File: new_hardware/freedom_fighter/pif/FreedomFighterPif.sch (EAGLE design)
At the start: 15 parts, among them U1 PIA6821, U4 HD68A09EP, U5 74LS74D, U9 DM74LS04N

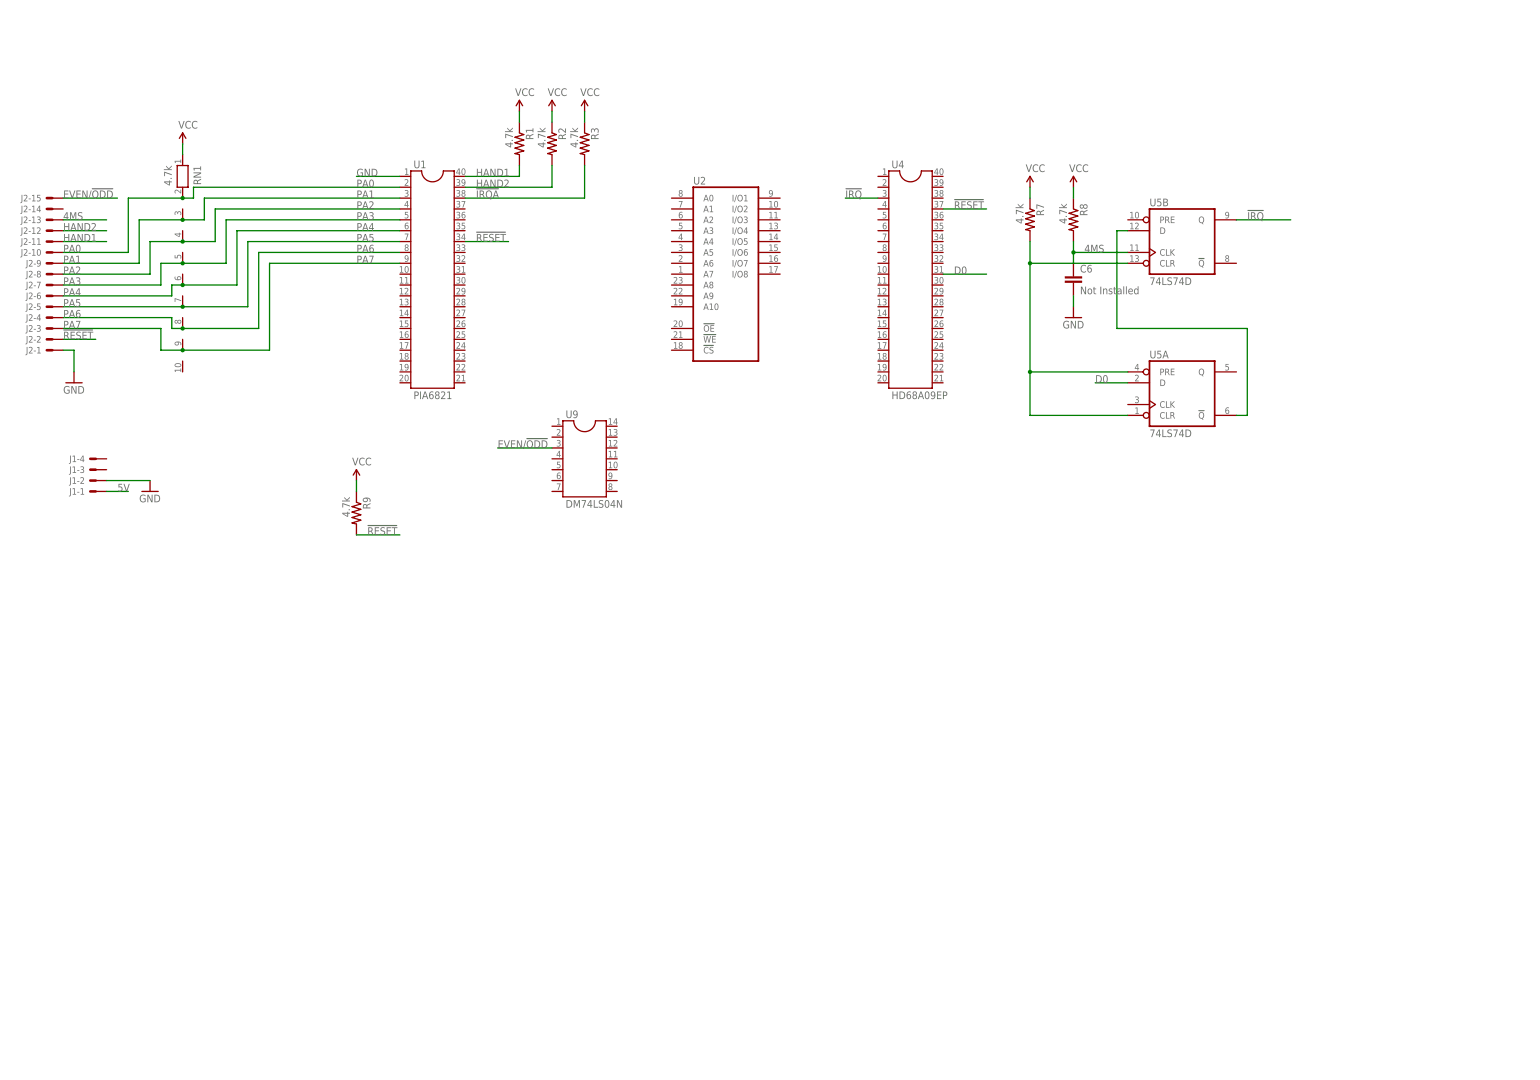
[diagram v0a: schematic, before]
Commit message: did more reverse engineering of freedom fighter pif board
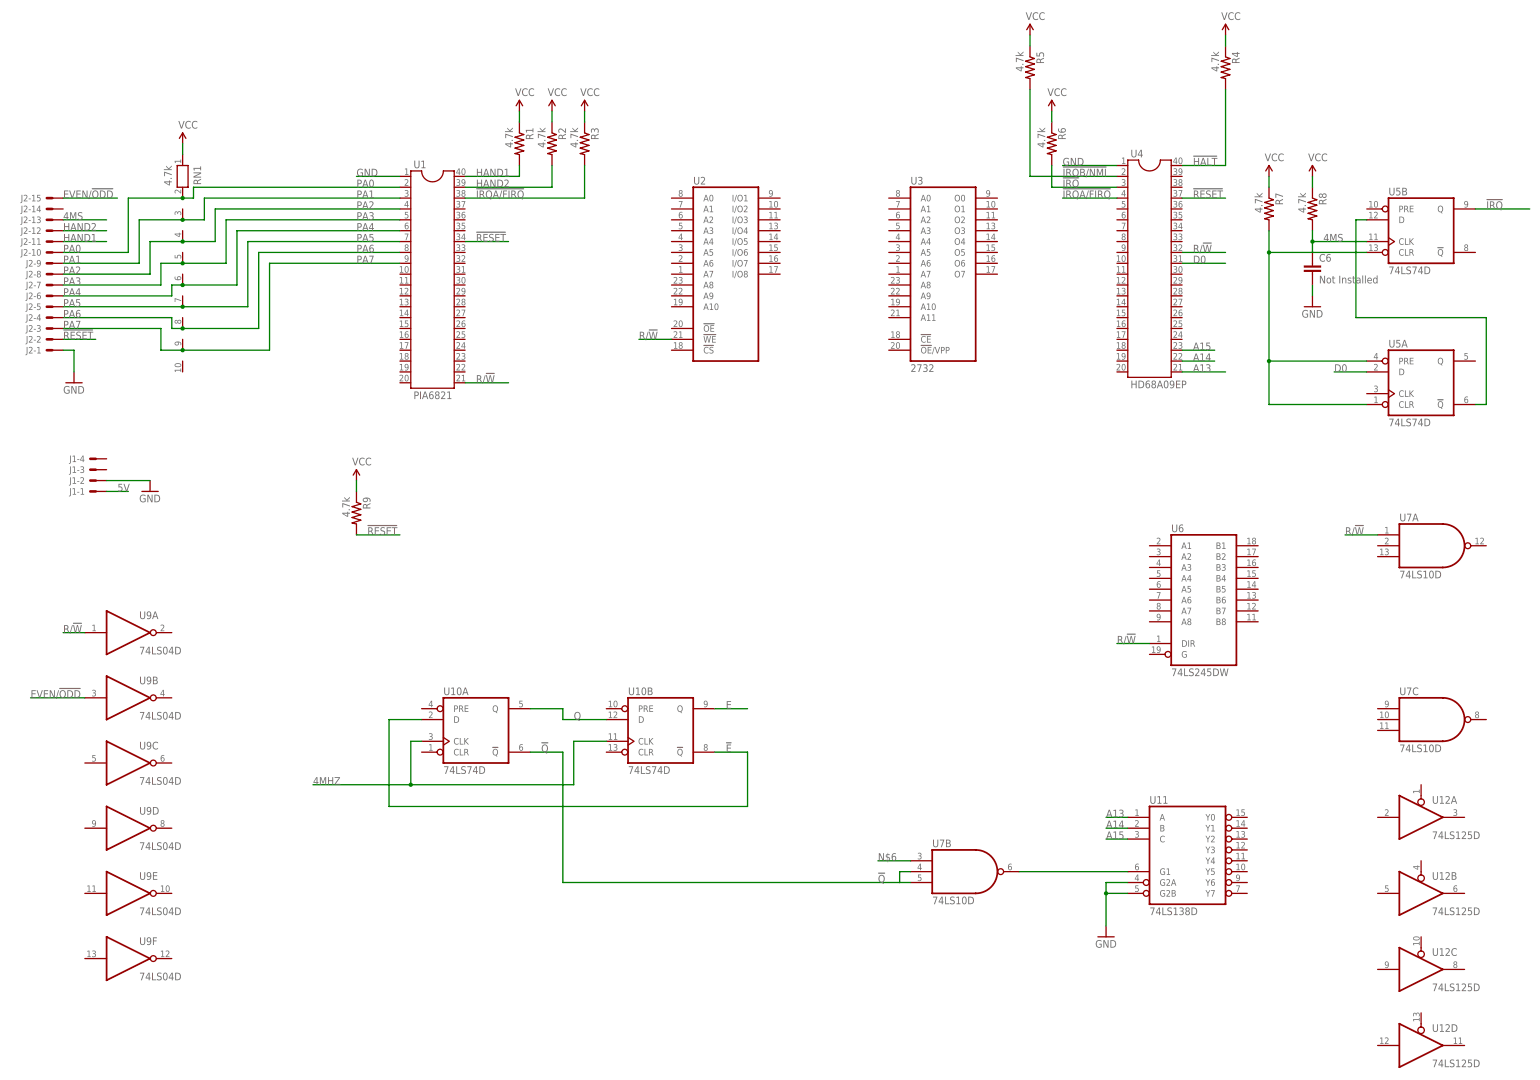
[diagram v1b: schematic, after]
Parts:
- added R4, R5, R6: 4.7k, SparkFun:RESISTOR1206
- added U10: 74LS74D, 74xx-us:74LS74D
- added U11: 74LS138D, 74xx-us:74LS138D
- added U12: 74LS125D, 74xx-eu:74LS125D
- added U3: 2732, memory:2732
- added U6: 74LS245DW, 74xx-us:74LS245DW
- added U7: 74LS10D, 74xx-us:74LS10D
- U9: value DM74LS04N -> 74LS04D; device ic-package:DIL14 -> 74xx-us:74LS04D
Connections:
- removed net !IRQA: R3.2, U1.38
- new net !E: U10A.D, U10B.!Q
- new net !HALT: R4.2, U4.40
- new net !IRQA/FIRQ: R3.2, U1.38, U4.4
- new net !IRQB/NMI: R5.2, U4.2
- new net !Q: U10A.!Q, U7B.I1, U7B.I2
- new net 4MHZ: U10A.CLK, U10B.CLK
- new net A13: U11A.A, U4.21
- new net A14: U11A.B, U4.22
- new net A15: U11A.C, U4.23
- new net E: U10B.Q
- new net N$4: U11A.G1, U7B.O
- new net N$6: U7B.I0
- new net Q: U10A.Q, U10B.D
- new net R/!W: U1.21, U2G$1.!WE, U4.32, U6A.DIR, U7A.I0, U9A.I
- net !IRQ: now also R6.2
- net EVEN/!ODD: now also U9B.I; no longer U9.3
- net GND: now also U11A.G2A, U11A.G2B, U4.1
- net VCC: now also R4.1, R5.1, R6.1
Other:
- moved on the sheet: C6, R7, R8, U4, U5A, U5B

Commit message: more reverse engineering
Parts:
- removed U3: 2732, memory:2732
- added C100: Unknown value, SparkFun:CAP1206
- added DB1: DB25, mpo:A32077-ND
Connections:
- removed net N$6: U7B.I0
- new net !ENABLE_DAVDAK: U11A.Y1, U12A.OE, U12D.OE
- new net !ENABLE_PIA: U1.23, U11A.Y4
- new net !ENABLE_RAM: U11A.Y0, U2G$1.!CS
- new net !ENABLE_ROM: U11A.Y7, U12B.OE
- new net !ENABLE_ROM_CE: U12B.O
- new net !ENABLE_U12C: U11A.Y6, U12C.OE
- new net !ENABLE_VP931_DATA: U11A.Y3, U6A.G, U9D.I
- new net !VP931_RDEN: DB1.10, U7A.O
- new net !VP931_WREN: DB1.22, U7C.O
- new net D1: U4.30, U6A.B2
- new net D2: U4.29, U6A.B3
- new net D3: U4.28, U6A.B4
- new net D4: U4.27, U6A.B5
- new net D5: U4.26, U6A.B6
- new net D6: U12D.O, U4.25, U6A.B7
- new net D7: U12A.O, U4.24, U6A.B8
- new net ENABLE_VP931_DATA: U7A.I2, U7C.I1, U9D.O
- new net VP931_D0: DB1.14, U6A.A1
- new net VP931_D1: DB1.15, U6A.A2
- new net VP931_D2: DB1.16, U6A.A3
- new net VP931_D3: DB1.17, U6A.A4
- new net VP931_D4: DB1.18, U6A.A5
- new net VP931_D5: DB1.19, U6A.A6
- new net VP931_D6: DB1.20, U6A.A7
- new net VP931_D7: DB1.21, U6A.A8
- new net VP931_DAK: DB1.23, U12A.I
- new net VP931_DAV: DB1.11, U12D.I
- new net W/!R: U2G$1.!OE, U7C.I0, U9A.O
- net !E: now also U7B.I0
- net D0: now also U6A.B1
- net E: now also C100.2, U4.34, U7A.I1
- net GND: now also DB1.9, U12B.I, U12C.I, U5B.PRE
- net Q: now also U4.35, U7C.I2
- net VCC: now also C100.1
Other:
- note added: "N/C?"
- note added: "This circuit is installed but does nothing because pin 10 is grounded"
- note added: "U3 is a 27128D!"
- moved on the sheet: U11

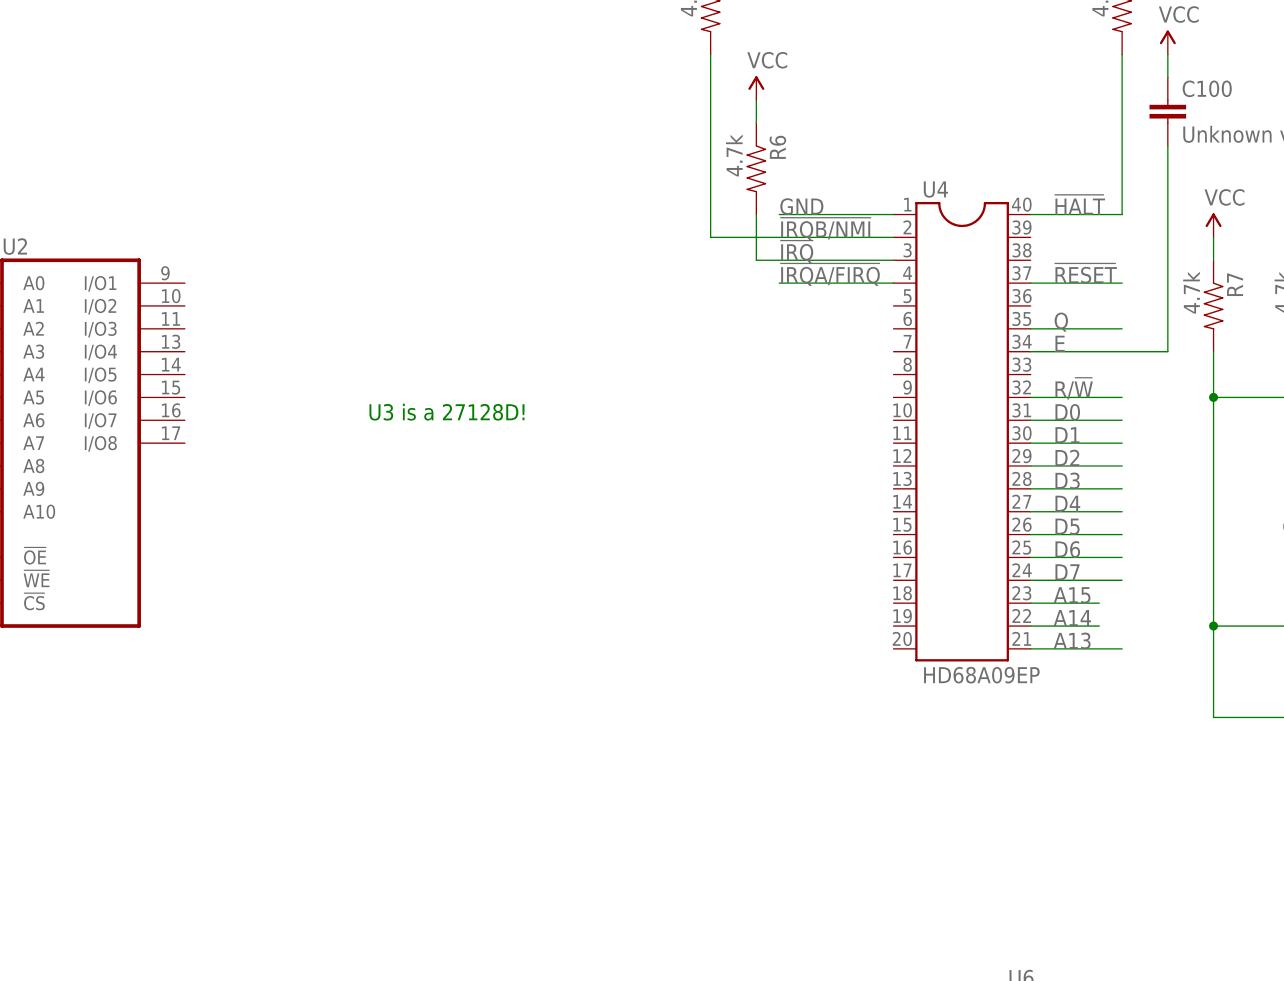
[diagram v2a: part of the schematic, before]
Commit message: added FFR PIF disassembly and updated PIF schematics
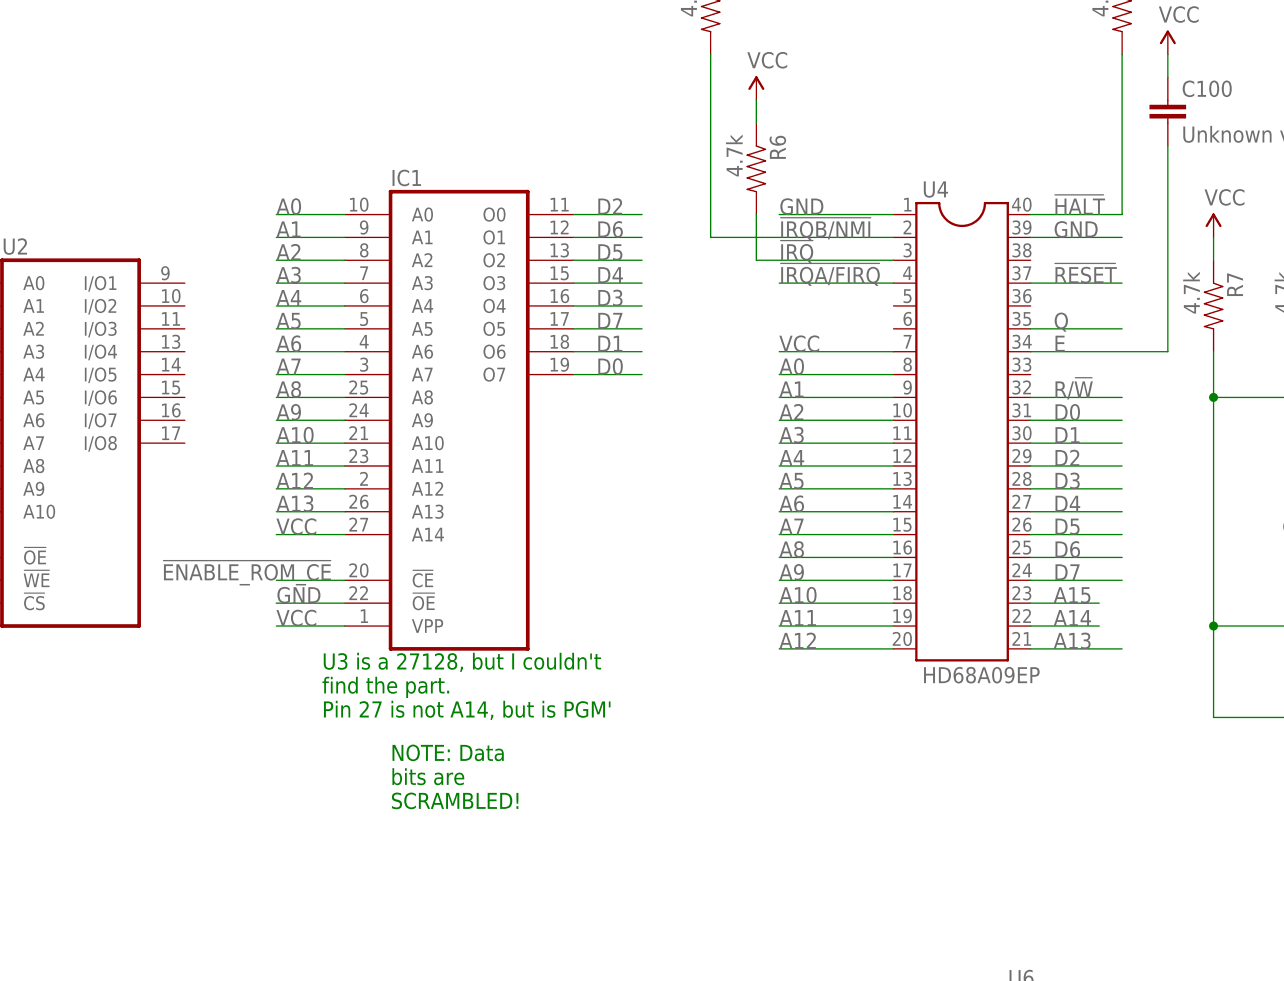
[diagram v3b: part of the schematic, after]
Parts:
- added IC1: (no value), memory:27256
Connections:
- new net A0: IC1A.A0, U4.8
- new net A1: IC1A.A1, U4.9
- new net A10: IC1A.A10, U4.18
- new net A11: IC1A.A11, U4.19
- new net A12: IC1A.A12, U4.20
- new net A2: IC1A.A2, U4.10
- new net A3: IC1A.A3, U4.11
- new net A4: IC1A.A4, U4.12
- new net A5: IC1A.A5, U4.13
- new net A6: IC1A.A6, U4.14
- new net A7: IC1A.A7, U4.15
- new net A8: IC1A.A8, U4.16
- new net A9: IC1A.A9, U4.17
- net !ENABLE_ROM_CE: now also IC1A.!CE
- net A13: now also IC1A.A13
- net D0: now also IC1A.O7
- net D1: now also IC1A.O6
- net D2: now also IC1A.O0
- net D3: now also IC1A.O4
- net D4: now also IC1A.O3
- net D5: now also IC1A.O2
- net D6: now also IC1A.O1
- net D7: now also IC1A.O5
- net GND: now also IC1A.!OE, U4.39
- net VCC: now also IC1A.A14, IC1A.VPP, U4.7
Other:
- note added: "NOTE: Data bits are SCRAMBLED!"
- note added: "U3 is a 27128, but I couldn't find the part. Pin 27 is not A14, but is PGM'"
- note removed: "U3 is a 27128D!"

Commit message: almost done with schematic, did some more disassembling
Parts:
- added C14, C9: 0.001uF, SparkFun:CAP1206
- added C15: 100uF/25V, SparkFun:CAP_POLPTH2
- added L1: 2.2uH, rcl:L-USTJ8-U2
- added R10, R11, R12: 4.7k, SparkFun:RESISTOR1206
- added X1: CRYSTAL OSC, crystal:TC46C
- DB1: value DB25 -> DB25 (FEMALE)
- U2: value (none) -> HM6116P-A
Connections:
- net !ENABLE_U12C renamed !ENABLE_ROM_C_TO_D
- removed net !ENABLE_ROM_CE: IC1A.!CE, U12B.O
- removed net 5V: J1-1.S
- new net !ENABLE_ROM_E_TO_F: U11A.Y7, U12B.OE
- new net CS0/CS1: R10.2, U1.22, U1.24
- new net N$5: R11.2, U10A.CLR, U10A.PRE, U10B.CLR, U10B.PRE
- new net N$8: C9.2, J1-1.S, L1.1
- net !ENABLE_ROM: now also IC1A.!CE, R12.2, U12B.O, U12C.O; no longer U11A.Y7, U12B.OE
- net !IRQB/NMI: now also U1.37
- net 4MHZ: now also X1.OUT
- net A0: now also U1.36, U2G$1.A0
- net A1: now also U1.35, U2G$1.A1
- net A10: now also U2G$1.A10
- net A2: now also U2G$1.A2
- net A3: now also U2G$1.A3
- net A4: now also U2G$1.A4
- net A5: now also U2G$1.A5
- net A6: now also U2G$1.A6
- net A7: now also U2G$1.A7
- net A8: now also U2G$1.A8
- net A9: now also U2G$1.A9
- net D0: now also U1.33, U2G$1.I/O1
- net D1: now also U1.32, U2G$1.I/O2
- net D2: now also U1.31, U2G$1.I/O3
- net D3: now also U1.30, U2G$1.I/O4
- net D4: now also U1.29, U2G$1.I/O5
- net D5: now also U1.28, U2G$1.I/O6
- net D6: now also U1.27, U2G$1.I/O7
- net D7: now also U1.26, U2G$1.I/O8
- net E: now also U1.25
- net GND: now also C14.1, C15.-, C9.1, X1.GND
- net VCC: now also C14.2, C15.+, L1.2, R10.1, R11.1, R12.1, U1.20, X1.VCC
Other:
- note added: "10-15 and 18-19 mirror Star Rider PIF exactly, going to an uninstalled 244. Pins 16-17 are N/C from what I can tell."
- note added: "Freedom Fighter PIF Prototype"
- note added: "I double checked: Pin 10 and Pin 13 are not connected"
- note added: "I partly guessed on the values for C9 and C14, and L1 by using Star Rider as reference."
- note added: "NOTE: DAV' is unconnected. This is opposite of Firefox, which uses DAV' but ignores DAV."
- note added: "NOTE: Data bits are SCRAMBLED (a simple type of obfuscation?)."
- note added: "NOTE: There is an uninstalled IC (U8) and uninstalled set of pin headers (J3) that look to be leftover from Star Rider's design. I did not bother with these since they were never used. They most likely mirror very closely the Star Rider PIF schematic."
- note added: "Oscillator is 4 MHz. I didn't try to find an exact match, just enough to document."
- note added: "Reverse engineered by Matt Ownby 2015"
- note added: "U3 is a 27128, but I couldn't find the part so I used a 27256. Pin 27 is not A14, but is PGM'"
- note removed: "NOTE: Data bits are SCRAMBLED!"
- note removed: "U3 is a 27128, but I couldn't find the part. Pin 27 is not A14, but is PGM'"
- moved on the sheet: C6, R7, R8, R9, U10A, U10B, U5A, U5B

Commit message: Essentially finished schematic, started laying out PCB
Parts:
- removed X1: CRYSTAL OSC, crystal:TC46C
- added C1, C10, C11, C12, C13, C2, C3, C4, C5, C7, C8: 0.1uF, SparkFun:CAP1206
- added JP1, JP4: (no value), pinhead:PINHD-1X20
- added JP2, JP5, JP6: (no value), pinhead:PINHD-1X8
- added JP3: (no value), pinhead:PINHD-1X2
- added JP7, JP8: (no value), pinhead:PINHD-1X7
- added U$1: OSCILLATOR-SMT4, mpo:OSCILLATOR-SMT4
- L1: device rcl:L-USTJ8-U2 -> SparkFun:INDUCTOR1206H*
- renumbered IC1 to U3
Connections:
- net !ENABLE_DAVDAK: now also JP6.3
- net !ENABLE_PIA: now also JP6.6
- net !ENABLE_RAM: now also JP6.2
- net !ENABLE_ROM_C_TO_D: now also JP6.8
- net !ENABLE_ROM_E_TO_F: now also JP5.7
- net !ENABLE_VP931_DATA: now also JP6.5, JP8.6
- net !HALT: now also JP4.1
- net !IRQ: now also JP1.3
- net !IRQA/FIRQ: now also JP1.4
- net !IRQB/NMI: now also JP1.2
- net !RESET: now also JP4.4
- net 4MHZ: now also U$1.OUT; no longer X1.OUT
- net A0: now also JP1.8
- net A1: now also JP1.9
- net A10: now also JP1.18
- net A11: now also JP1.19
- net A12: now also JP1.20
- net A13: now also JP4.20
- net A14: now also JP4.19
- net A15: now also JP4.18
- net A2: now also JP1.10
- net A3: now also JP1.11
- net A4: now also JP1.12
- net A5: now also JP1.13
- net A6: now also JP1.14
- net A7: now also JP1.15
- net A8: now also JP1.16
- net A9: now also JP1.17
- net D0: now also JP4.10
- net D1: now also JP4.11
- net D2: now also JP4.12
- net D3: now also JP4.13
- net D4: now also JP4.14
- net D5: now also JP4.15
- net D6: now also JP4.16
- net D7: now also JP4.17
- net E: now also JP4.7
- net ENABLE_VP931_DATA: now also JP8.7
- net EVEN/!ODD: now also JP7.3
- net GND: now also C1.2, C10.2, C11.2, C12.2, C13.2, C2.2, C3.2, C4.2, C5.2, C7.2, C8.2, JP1.1, JP5.8, JP7.7, U$1.GND; no longer X1.GND
- net HAND1: now also JP3.1
- net HAND2: now also JP3.2
- net PA0: now also JP2.1
- net PA1: now also JP2.2
- net PA2: now also JP2.3
- net PA3: now also JP2.4
- net PA4: now also JP2.5
- net PA5: now also JP2.6
- net PA6: now also JP2.7
- net PA7: now also JP2.8
- net Q: now also JP4.6
- net R/!W: now also JP4.9, JP7.1
- net VCC: now also C1.1, C10.1, C11.1, C12.1, C13.1, C2.1, C3.1, C4.1, C5.1, C7.1, C8.1, JP1.7, JP6.1, JP8.1, U$1.ENABLE, U$1.VCC; no longer X1.VCC
- net W/!R: now also JP7.2
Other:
- note added: "A resistor or cap connecting 'E' to VCC. Still working on discovering this value."
- note added: "M6809E test points"
- note added: "Oscillator is 4 MHz. I didn't try to find an exact match, just enough to document. The pins on the board mirror the Star Rider PIF board, which is not reflected here."
- note added: "PIA Test Points"
- note added: "Test Points"
- note added: "U11 Test Points"
- note added: "U9 test points"
- note removed: "Oscillator is 4 MHz. I didn't try to find an exact match, just enough to document."
